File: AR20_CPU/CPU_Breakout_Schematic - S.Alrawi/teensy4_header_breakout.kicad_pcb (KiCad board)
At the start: 4 copper layers, 65 x 74 mm, 75 parts, among them SW1 SW_SPST, U1 74LCX125M, U2 MCP1700_SOT23

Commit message: 4 Layers PCB is 90% finished
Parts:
- removed H3: MountingHole, MountingHole:MountingHole_2.5mm_Pad
- removed MX34: MX34_36_pins, Teensy_Footprint_Library:Connector_MX34_36pins
- removed MX34_Housing1: MX34_Housing, Teensy_Footprint_Library:Housing_3pins
- removed Teensy4.0: Teensy_pins, Teensy_Footprint_Library:Teensy_40_footprint
- added C19: ?, Capacitor_SMD:C_0603_1608Metric, B.Cu at (130.7, 91.6)
- added D9: 3V, Diode_SMD:D_0603_1608Metric, B.Cu at (127.7, 96.2)
- added H7: MountingHole, MountingHole:MountingHole_2.5mm_Pad, F.Cu at (172.6, 142.6)
- added JP10: SolderJumper_2_Open, Jumper:SolderJumper-2_P1.3mm_Open_RoundedPad1.0x1.5mm, B.Cu at (130.7, 93.9)
- added MX1: MX34_36_pins, Teensy_Footprint_Library:Connector_MX34_36pins, F.Cu at (143.1, 140.7)
- added OpAmp1: NCV20091SQ3T2G, Teensy_Footprint_Library:SC−70_NCV20091SQ3T2G, B.Cu at (140.5, 80.2)
- added R21: ?, Resistor_SMD:R_0603_1608Metric, B.Cu at (129.8, 87.9)
- added R22: ?, Resistor_SMD:R_0603_1608Metric, B.Cu at (130.7, 89.6)
- added Teensy4.1: Teensy_pins, Teensy_Footprint_Library:Teensy_40_footprint, F.Cu at (126.4, 118.4)
- BT1: value 2.7V -> 3V cell coin
- C11: value 10u -> 100u
- C12, C13: value 0.1u -> 100u
- C15: value 10u -> 0.1u
- C16: value 100u -> 0.1u
- C17, C18: value 100u -> 10u
- H1: value GND -> CANH_out; footprint MountingHole:MountingHole_2.5mm_Pad -> TestPoint:TestPoint_THTPad_D1.5mm_Drill0.7mm
- H2: value MountingHole -> CANL_out; footprint MountingHole:MountingHole_2.5mm_Pad -> TestPoint:TestPoint_THTPad_D1.5mm_Drill0.7mm
- H5: value CANH_out -> MountingHole; footprint TestPoint:TestPoint_THTPad_D1.5mm_Drill0.7mm -> MountingHole:MountingHole_2.5mm_Pad
- H6: value CANL_out -> MountingHole; footprint TestPoint:TestPoint_THTPad_D1.5mm_Drill0.7mm -> MountingHole:MountingHole_2.5mm_Pad
- R17: value 10k -> 60; footprint Resistor_SMD:R_0603_1608Metric -> Resistor_SMD:R_0603_1608Metric_Pad1.05x0.95mm_HandSolder
- R18: value 10k -> 120; footprint Resistor_SMD:R_0603_1608Metric -> Resistor_SMD:R_0603_1608Metric_Pad1.05x0.95mm_HandSolder
- R19: value 60 -> 10k; footprint Resistor_SMD:R_0603_1608Metric_Pad1.05x0.95mm_HandSolder -> Resistor_SMD:R_0603_1608Metric
- R20: value 120 -> 10k; footprint Resistor_SMD:R_0603_1608Metric_Pad1.05x0.95mm_HandSolder -> Resistor_SMD:R_0603_1608Metric
- moved H6 67.8 mm to (113.6, 142.6)
- moved C11 53.7 mm to (170.8, 121.3), turned to 0 degrees
- moved C18 53.6 mm to (164.7, 126.2), turned to 0 degrees
- moved C16 53.2 mm to (118.2, 113.4)
- moved R18 48.8 mm to (168.3, 110.0), turned to 90 degrees
- moved R19 47.3 mm to (119.9, 104.1), turned to 0 degrees
- moved R17 46.3 mm to (166.0, 110.0), turned to 270 degrees
- moved C15 45.8 mm to (119.6, 119.6), turned to 90 degrees
- moved R20 45.4 mm to (117.6, 119.5), turned to 90 degrees
- moved SW1 38.3 mm to (123.9, 74.8), turned to 0 degrees
- moved H1 33.2 mm to (172.1, 108.5)
- moved H5 31.0 mm to (172.6, 74.6)
- moved H2 30.6 mm to (172.1, 106.0)
- moved JP9 13.8 mm to (166.8, 106.1), turned to 90 degrees
- moved C12 12.7 mm to (113.3, 109.9), turned to 0 degrees
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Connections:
- C11 pad 1: 12V_IN -> Vinn_5V
- C12 pad 1: 12V_IN -> Ground
- C12 pad 2: Ground -> Vinn_5V
- C13 pad 1: Vinn_5V -> Ground
- C13 pad 2: Ground -> 3V3_SD
- C14 pad 1: Vinn_5V -> 12V_IN
- C17 pad 1: Ground -> Vinn_5V
- C17 pad 2: Vinn_5V -> Ground
- C18 pad 1: Ground -> 12V_IN
- C18 pad 2: 3V3_SD -> Ground
- H1 pad 1: (no net) -> Net-(CANmodule1-Pad7)
- H2 pad 1: (no net) -> Net-(CANmodule1-Pad6)
- H5 pad 1: Net-(CANmodule1-Pad7) -> (no net)
- H6 pad 1: Net-(CANmodule1-Pad6) -> (no net)
- R17 pad 1: 12V_IN -> Ground
- R17 pad 2: Net-(R17-Pad2) -> Net-(CANmodule1-Pad8)
- R18 pad 1: 3V3_SD -> Net-(CANmodule1-Pad7)
- R18 pad 2: 12_MISO -> Net-(JP9-Pad1)
- R19 pad 1: Ground -> 3V3_SD
- R19 pad 2: Net-(CANmodule1-Pad8) -> 12_MISO
- R20 pad 1: Net-(CANmodule1-Pad7) -> 12V_IN
- R20 pad 2: Net-(JP9-Pad1) -> Net-(R20-Pad2)
- SWReg_NVC1 pad 4: Net-(R17-Pad2) -> Net-(R20-Pad2)
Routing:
- net Sensor_Input_1: track 0.00 -> 72.9 mm, vias 0 -> 2
- net Sensor_Input_2: track 0.00 -> 67.8 mm, vias 0 -> 2
- net ON_OFF: track 0.00 -> 62.3 mm, vias 0 -> 2
- net Sensor_Input_8: track 0.00 -> 50.8 mm, vias 0 -> 2
- net Sensor_Input_4: track 0.00 -> 48.4 mm, vias 0 -> 2
- net 24_A10: track 19.3 -> 66.8 mm, vias 0 -> 2
- net Sensor_Input_5: track 0.00 -> 47.1 mm, vias 0 -> 2
- net Sensor_Input_7: track 0.00 -> 44.4 mm, vias 0 -> 2
- net Sensor_Input_3: track 0.00 -> 42.0 mm, vias 0 -> 2
- net Sensor_Input_6: track 0.00 -> 41.0 mm, vias 0 -> 2
- net Ground: track 0.00 -> 38.9 mm, vias 0 -> 34
- net 25_A11: track 22.4 -> 43.7 mm
- net 28_RX7: track 49.2 -> 28.1 mm, vias 0 -> 2
- net 33_MCLK2: track 42.8 -> 23.0 mm
- net 26_A12: track 26.8 -> 43.3 mm, vias 2 -> 0
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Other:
- board size 65 x 74 mm -> 65 x 77 mm
- board text added: "YOLO-AR20"

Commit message: BreakoutBoard final edit
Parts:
- removed R19: 10k, Resistor_SMD:R_0603_1608Metric
- removed U1: 74LCX125M, SamacSys_Parts:SOIC127P600X175-14N
- C12: value 100u -> 0.1u
- C13: value 100u -> 1u
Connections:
- net 3V3_SD renamed 3V3_OUT
- SDcard1 pad 2: CS_3.3V -> 10_CS
- SDcard1 pad 3: MOSI_3.3V -> 11_MOSI
- SDcard1 pad 5: SCLK_3.3V -> 13(LED)
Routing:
- net SCLK_3.3V: track 20.8 -> 0.00 mm, vias 2 -> 0
- net MOSI_3.3V: track 11.7 -> 0.00 mm
- net CS_3.3V: track 11.4 -> 0.00 mm, vias 2 -> 0
- net Ground: track 38.9 -> 27.6 mm, vias 34 -> 33
- net 13(LED): track 52.1 -> 63.3 mm, vias 2 -> 1
- net 10_CS: track 52.0 -> 62.9 mm
- net 11_MOSI: track 62.0 -> 71.0 mm
- net 3V3_OUT: track 33.6 -> 25.3 mm, vias 2 -> 1
- net Vinn_5V: track 154.3 -> 155.5 mm
- net 12V_IN: track 72.0 -> 71.4 mm
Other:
- board text added: "1"
- board text added: "2"
- board text added: "3"
- board text added: "4"

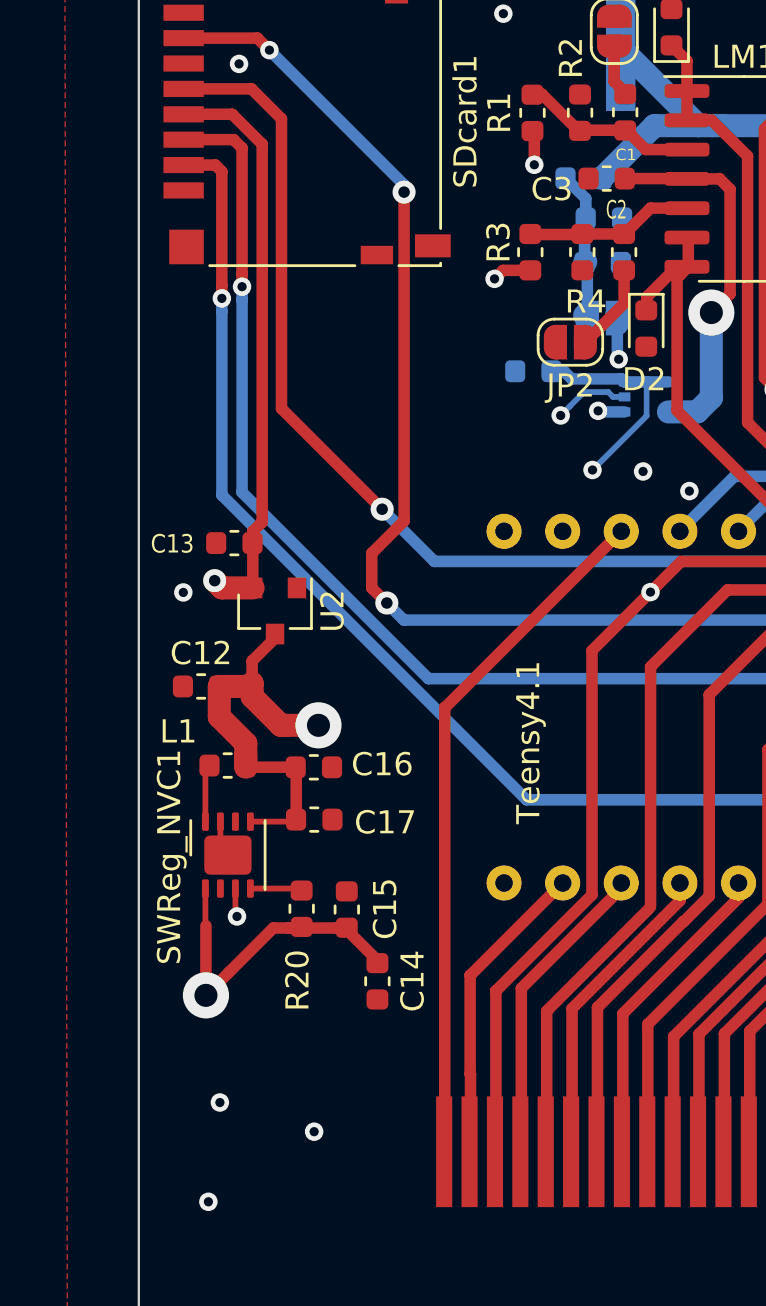
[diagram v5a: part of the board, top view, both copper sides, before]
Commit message: Edited the Vreg  to SD
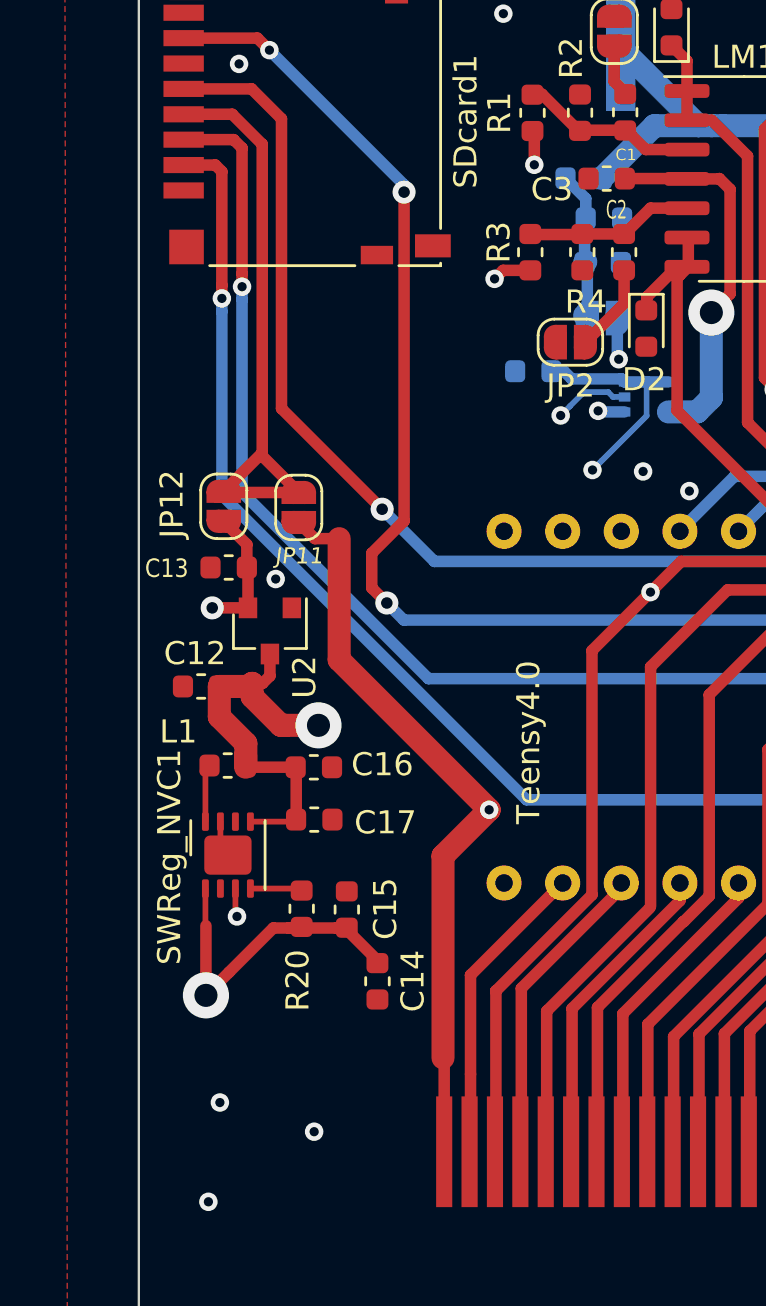
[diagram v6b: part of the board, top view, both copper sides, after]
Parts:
- added JP11: SolderJumper_2_Open, Jumper:SolderJumper-2_P1.3mm_Open_RoundedPad1.0x1.5mm, F.Cu at (117.5, 102.2)
- added JP12: SolderJumper_2_Open, Jumper:SolderJumper-2_P1.3mm_Open_RoundedPad1.0x1.5mm, F.Cu at (114.2, 102.1)
- moved C13 1.09 mm to (114.5, 104.8)
- moved U2 0.89 mm to (116.2, 107.5)
- renumbered Teensy4.1 to Teensy4.0
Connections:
- SDcard1 pad 4: 3V3_OUT -> Net-(JP11-Pad1)
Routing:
- net Net-(JP11-Pad1): track 0.00 -> 25.3 mm
- net 3V3_OUT: track 25.3 -> 5.73 mm
- net 3.3V: track 30.5 -> 46.6 mm, vias 0 -> 1

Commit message: Edited
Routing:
- net ON_OFF: track 62.4 -> 59.7 mm
